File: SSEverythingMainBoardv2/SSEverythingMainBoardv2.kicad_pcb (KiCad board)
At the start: 2 copper layers, 99.1 x 81.3 mm, 70 parts, among them J1 CONN_06SILK_FEMALE_PTH, J2 CONN_06SILK_FEMALE_PTH, J3 POWER, J4 Switch, J5 Conn_01x02, J6 Conn_01x05, M1 Left MOTOR, M2 Right MOTOR, SW1 TACT_SW, U1 DFRobot_DC_Controller

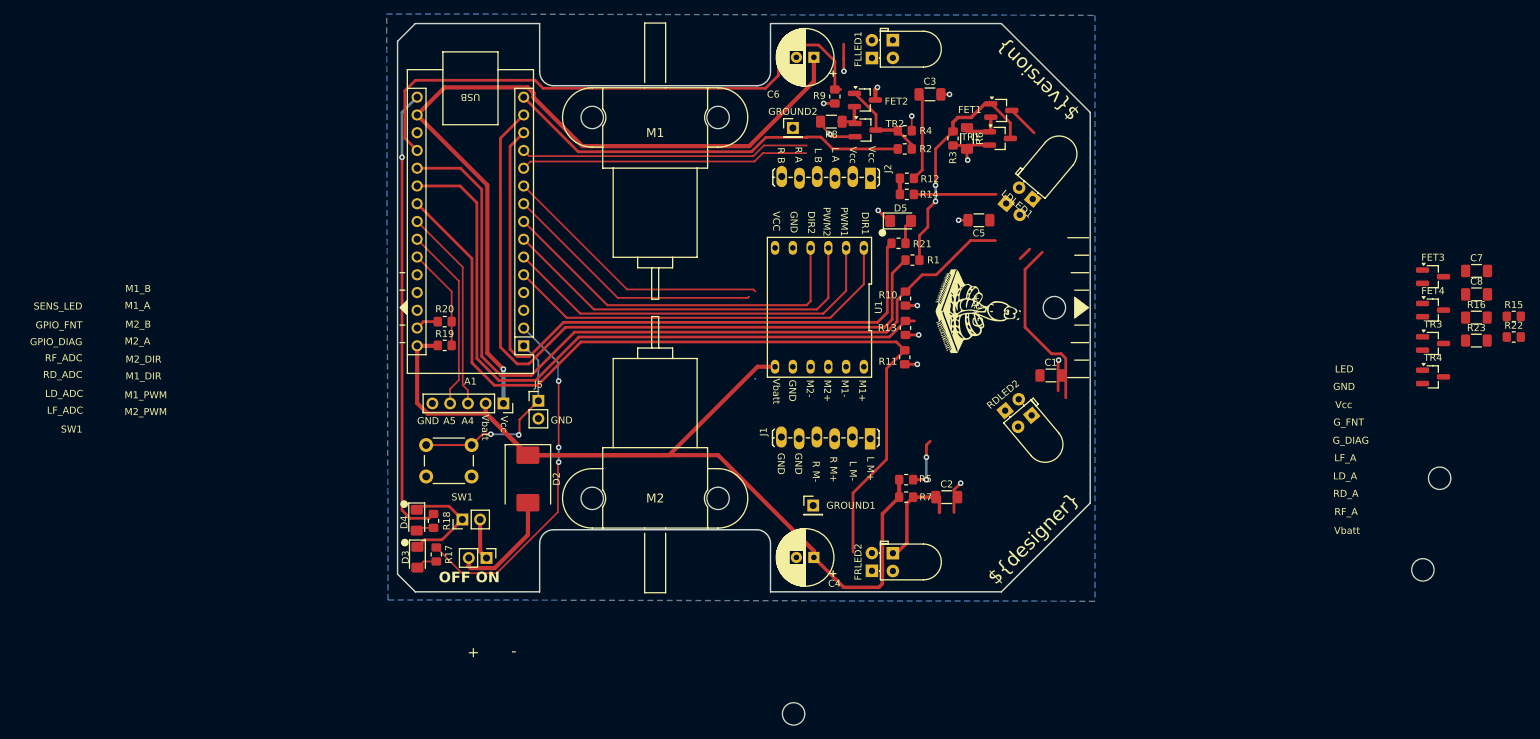
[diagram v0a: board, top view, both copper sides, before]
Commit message: before updating to KiCad 9 and changing sensor design
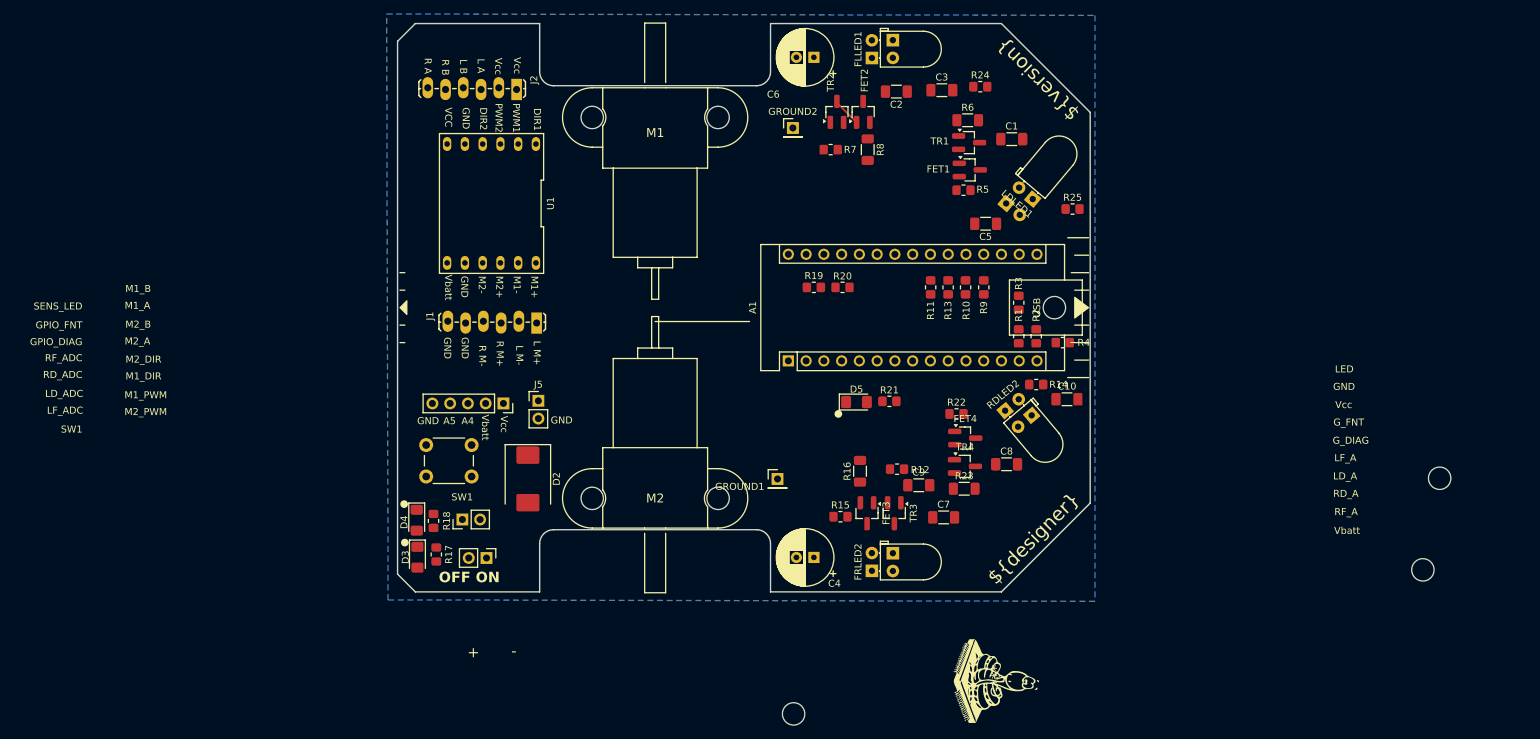
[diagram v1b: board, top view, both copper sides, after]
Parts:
- added C10: 10uF, Capacitor_SMD:C_1206_3216Metric_Pad1.33x1.80mm_HandSolder, F.Cu at (163.9, 118.1)
- added C9: 10uF, Capacitor_SMD:C_1206_3216Metric_Pad1.33x1.80mm_HandSolder, F.Cu at (142.7, 130.4)
- added R24: 220R, Resistor_SMD:R_0805_2012Metric_Pad1.20x1.40mm_HandSolder, F.Cu at (151.5, 73.4)
- added R25: 220R, Resistor_SMD:R_0805_2012Metric_Pad1.20x1.40mm_HandSolder, F.Cu at (164.7, 90.9)
- R15, R22, R5, R7: value 10R -> 220R
- moved R15 100.5 mm to (131.5, 134.9)
- moved R16 90.8 mm to (134.3, 128.4), turned to 90 degrees
- moved FET3 87.7 mm to (135.3, 134.4), turned to -90 degrees
- moved C7 84.0 mm to (146.3, 135.0)
- moved TR3 80.8 mm to (139.2, 134.4), turned to -90 degrees
- moved R22 80.5 mm to (148.1, 120.2)
- moved R23 76.3 mm to (149.2, 130.9)
- moved C8 71.5 mm to (155.3, 127.4)
- moved FET4 69.4 mm to (149.3, 123.7)
- moved TR4 68.2 mm to (149.3, 127.7)
- moved C2 58.4 mm to (139.5, 74.1), turned to 180 degrees
- moved R20 57.1 mm to (131.8, 102.1), turned to 0 degrees
- moved R19 53.4 mm to (127.7, 102.1)
- moved G*** 53.0 mm to (153.8, 158.4)
- moved J2 52.2 mm to (85.2, 73.8)
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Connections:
- A1 pad 5: LEFT_MOTOR_Dir -> RIGHT_MOTOR_Dir
- A1 pad 6: LEFT_MOTOR_PWM -> RIGHT_MOTOR_PWM
- A1 pad 7: RIGHT_MOTOR_PWM -> LEFT_MOTOR_PWM
- A1 pad 8: RIGHT_MOTOR_Dir -> LEFT_MOTOR_Dir
- C3 pad 2: GND -> Net-(C3-Pad2)
- C5 pad 2: GND -> Net-(C5-Pad2)
- J2 pad 5: RIGHT_ENC_A -> RIGHT_ENC_B
- J2 pad 6: RIGHT_ENC_B -> RIGHT_ENC_A
- R10 pad 2: GND -> Net-(C5-Pad2)
- R12 pad 1: Net-(LFPD1-C) -> Net-(RFPD1-C)
- R14 pad 1: Net-(LDPD1-C) -> Net-(RDPD1-C)
- R9 pad 2: GND -> Net-(C3-Pad2)
- RDPD1 pad 1: Net-(LDPD1-C) -> Net-(RDPD1-C)
- RFPD1 pad 1: Net-(LFPD1-C) -> Net-(RFPD1-C)
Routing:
- net Vbatt: track 155.8 -> 0.00 mm
- net RIGHT_FRONT_ADC: track 124.2 -> 0.00 mm
- net LEFT_DIAG_ADC: track 118.8 -> 0.00 mm
- net Vcc: track 118.2 -> 0.00 mm, vias 1 -> 0
- net GPIO_DIAG: track 103.5 -> 0.00 mm
- net RIGHT_DIAG_ADC: track 99.2 -> 0.00 mm
- net SENSOR_LED: track 98.9 -> 0.00 mm
- net LEFT_FRONT_ADC: track 81.7 -> 0.00 mm
- net GND: track 66.1 -> 0.00 mm, vias 11 -> 0
- net Net-(A1-D13/SCK): track 65.2 -> 0.00 mm, vias 1 -> 0
- net LEFT_MOTOR_Dir: track 58.4 -> 0.00 mm
- net GPIO_FRONT: track 58.3 -> 0.00 mm
- net LEFT_MOTOR_PWM: track 57.0 -> 0.00 mm
- net RIGHT_MOTOR_PWM: track 55.6 -> 0.00 mm
- net RIGHT_MOTOR_Dir: track 53.8 -> 0.00 mm
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
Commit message: first draft of new board all layout complete
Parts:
- removed FET1, FET2, FET3, FET4: SOT-23 DMG2302UK-7, Package_TO_SOT_SMD:SOT-23_Handsoldering
- removed R19: 180K, Resistor_SMD:R_0805_2012Metric_Pad1.20x1.40mm_HandSolder
- removed R20: 68K, Resistor_SMD:R_0805_2012Metric_Pad1.20x1.40mm_HandSolder
- removed TR1, TR2, TR3, TR4: BC849, Package_TO_SOT_SMD:SOT-23_Handsoldering
- added G***: LOGO, PBFootPrintLibrary:MicroPythonLogo, F.Cu at (139.7, 88.5)
- added Q1: PBSS4160DS, SamacSys_Parts:SOT95P275X110-6N, F.Cu at (134.8, 75.9)
- added Q2: PBSS4160DS, SamacSys_Parts:SOT95P275X110-6N, F.Cu at (133.7, 133.5)
- added Q3: PBSS4160DS, SamacSys_Parts:SOT95P275X110-6N, F.Cu at (150.4, 78.3)
- added Q4: PBSS4160DS, SamacSys_Parts:SOT95P275X110-6N, F.Cu at (148.8, 131.9)
- LDPD1, LFPD1, RDPD1, RFPD1: moved to F.Cu
- R1, R2: value 220R -> 1K
- R15, R22, R5, R7: value 220R -> 100R
- R16, R23, R6, R8: value R56 -> 2R
- moved R17 62.1 mm to (131.4, 117.4), turned to 0 degrees
- moved D3 60.1 mm to (126.4, 117.4), turned to 0 degrees
- moved R18 58.7 mm to (131.0, 124.9), turned to 0 degrees
- moved D4 56.3 mm to (126.2, 124.9), turned to 0 degrees
- moved J6 51.5 mm to (120.4, 83.0), turned to 0 degrees
- moved G*** 38.6 mm to (141.4, 121.8)
- moved R12 26.5 mm to (165.1, 121.0), turned to 90 degrees
- moved C10 24.1 mm to (144.9, 132.9), turned to 90 degrees
- moved R22 22.7 mm to (129.2, 132.7)
- moved R5 22.5 mm to (129.0, 78.2)
- moved R24 20.8 mm to (165.1, 89.2), turned to -90 degrees
- moved C5 17.6 mm to (146.0, 76.6), turned to -90 degrees
- moved C7 15.4 mm to (132.3, 141.4), turned to 90 degrees
- moved R4 12.9 mm to (152.3, 103.2), turned to 180 degrees
- moved C8 10.4 mm to (144.9, 127.7), turned to 90 degrees
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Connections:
- A1 pad 14: GPIO_DIAG -> GPIO_FRONT
- A1 pad 15: GPIO_FRONT -> GPIO_DIAG
- C3 pad 2: Net-(C3-Pad2) -> GND
- C5 pad 2: Net-(C5-Pad2) -> GND
- R10 pad 2: Net-(C5-Pad2) -> GND
- R9 pad 2: Net-(C3-Pad2) -> GND
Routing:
- net Vcc: track 0.00 -> 179.7 mm, vias 0 -> 1
- net Vbatt: track 0.00 -> 176.7 mm, vias 0 -> 2
- net LEFT_ENC_A: track 0.00 -> 93.8 mm
- net LEFT_ENC_B: track 0.00 -> 93.8 mm
- net RIGHT_ENC_A: track 0.00 -> 93.3 mm
- net RIGHT_ENC_B: track 0.00 -> 93.1 mm
- net GND: track 0.00 -> 92.0 mm, vias 0 -> 11
- net Net-(Q1A-B1): track 4.16 -> 80.1 mm, vias 0 -> 3
- net RIGHT_MOTOR_Dir: track 0.00 -> 72.7 mm
- net LEFT_MOTOR_Dir: track 0.00 -> 72.5 mm
- net LEFT_MOTOR_PWM: track 0.00 -> 72.4 mm
- net RIGHT_MOTOR_PWM: track 0.00 -> 72.2 mm
- net RIGHT_FRONT_ADC: track 0.00 -> 69.3 mm
- net Net-(Q3A-B1): track 0.00 -> 66.0 mm, vias 0 -> 3
- net Net-(A1-D1/TX): track 0.00 -> 56.8 mm
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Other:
- copper layers 2 -> 4
- board text added: "ON"
- board text removed: "OFF ON"

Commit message: First version of v4 board ready for production
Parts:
- M1: footprint ukmarsbot:MINI-METAL-GEARMOTOR-WITH-BRACKET_Alt -> ukmarsbot:MINI-METAL-GEARMOTOR-WITH-BRACKET
- M2: footprint ukmarsbot:MINI-METAL-GEARMOTOR-WITH-BRACKET -> ukmarsbot:MINI-METAL-GEARMOTOR-WITH-BRACKET_Alt
- moved GROUND1 49.9 mm to (72.9, 135.3)
- moved J5 38.9 mm to (125.7, 129.2), turned to 90 degrees
- moved J1 17.6 mm to (73.2, 116.6), turned to 90 degrees
- moved A1 2.85 mm to (121.2, 112.7)
- moved GROUND2 1.77 mm to (123.7, 78.7)
- moved G*** 1.63 mm to (139.8, 121.5)
- moved R18 0.30 mm to (131.3, 124.9)
- moved D3 0.14 mm to (126.3, 117.3)
- moved D4 0.14 mm to (126.3, 125.0)
- turned U1 to 180 degrees
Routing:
- net RIGHT_MOTOR_2: track 8.08 -> 30.9 mm
- net LEFT_MOTOR_Dir: track 72.5 -> 91.9 mm
- net Net-(A1-D1/TX): track 56.8 -> 75.5 mm
- net RIGHT_MOTOR_1: track 8.34 -> 27.1 mm
- net LEFT_MOTOR_2: track 8.08 -> 23.7 mm
- net RIGHT_MOTOR_Dir: track 72.7 -> 60.6 mm
- net LEFT_MOTOR_1: track 8.34 -> 19.9 mm
- net LEFT_MOTOR_PWM: track 72.4 -> 83.6 mm
- net GND: track 92.0 -> 102.8 mm
- net Vbatt: track 176.7 -> 183.8 mm, vias 2 -> 1
- net Net-(Q3A-B1): track 66.0 -> 70.4 mm
- net Vcc: track 179.7 -> 183.9 mm
- net LEFT_DIAG_ADC: track 28.9 -> 25.1 mm
- net RIGHT_MOTOR_PWM: track 72.2 -> 75.7 mm
- net SENSOR_LED: track 25.6 -> 22.7 mm
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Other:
- board text added: "L DIR"
- board text added: "L PWM"
- board text added: "R DIR"
- board text added: "R PWM"
- board text removed: "GPIO_DIAG"
- board text removed: "GPIO_FNT"
- board text removed: "LD_ADC"
- board text removed: "LED"
- board text removed: "LF_ADC"
- board text removed: "M1_A"
- board text removed: "M1_B"
- board text removed: "M1_DIR"
- board text removed: "M1_PWM"
- board text removed: "M2_A"
- board text removed: "M2_B"
- board text removed: "M2_DIR"
- board text removed: "M2_PWM"
- board text removed: "RD_ADC"
- board text removed: "RF_ADC"
- board text removed: "SENS_LED"
- board text removed: "SW1"

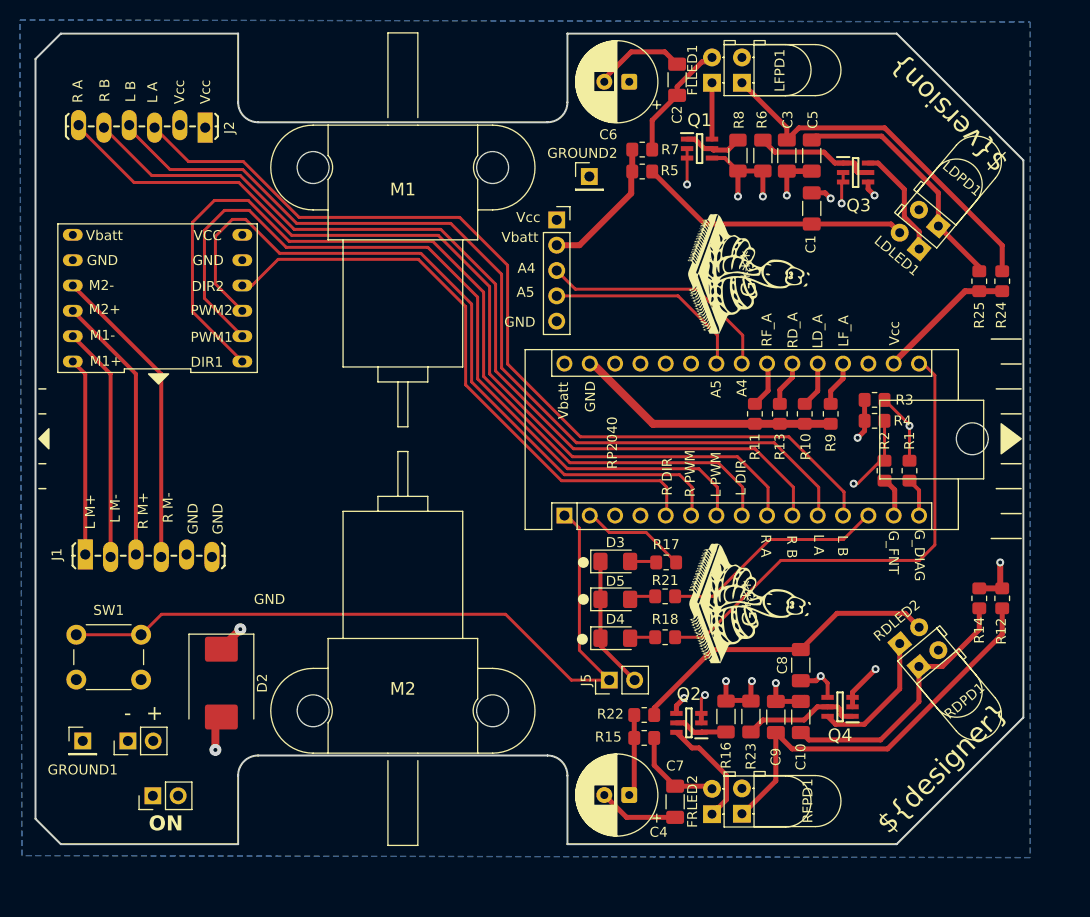
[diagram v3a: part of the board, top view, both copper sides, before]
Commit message: updated sensor locations, all resistors are back to be 0805, routing changes and moved the motor controller around plus other changes from Peter's suggestions
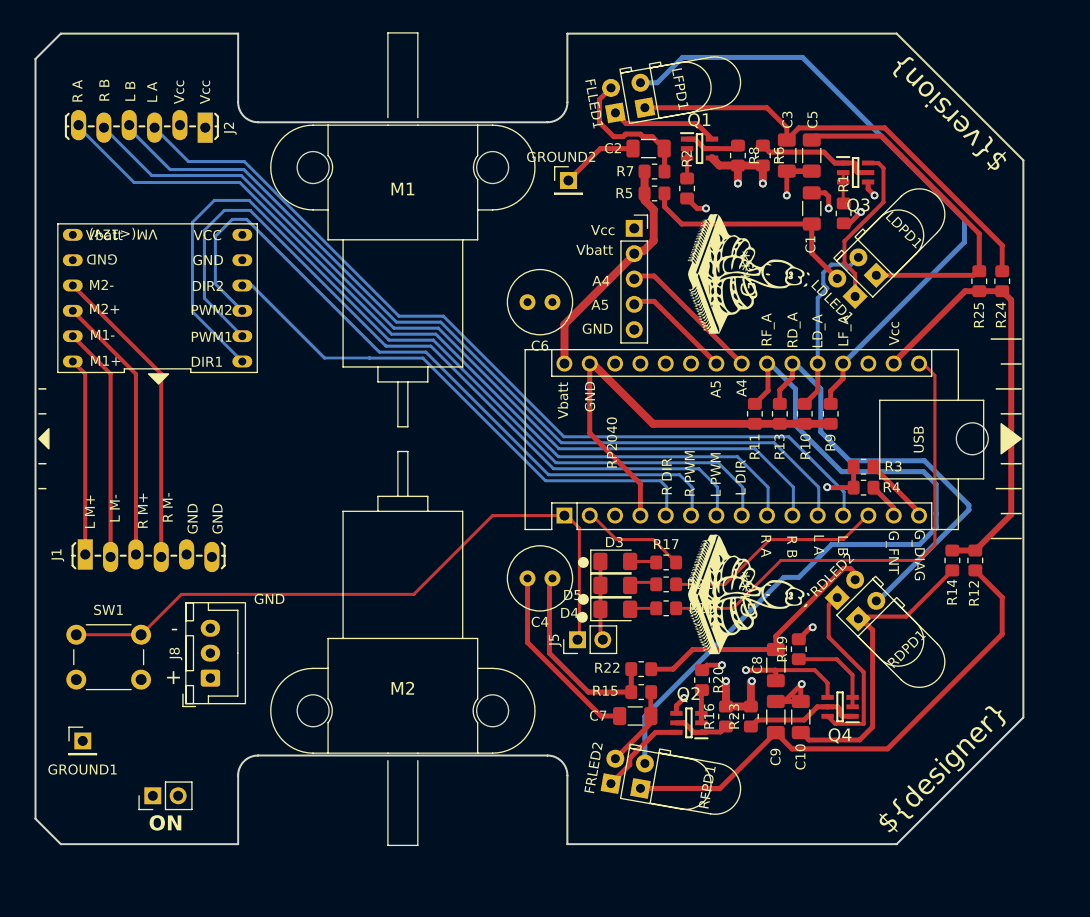
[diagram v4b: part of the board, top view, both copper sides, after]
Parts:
- removed D2: SS34, Diode_SMD:D_SMC
- removed J3: POWER, Connector_PinHeader_2.54mm:PinHeader_1x02_P2.54mm_Vertical
- added G***: LOGO, PBFootPrintLibrary:MicroPythonLogo, B.Cu at (80.7, 105.5)
- added J8: Conn_01x03, Connector_JST:JST_XH_B3B-XH-A_1x03_P2.50mm_Vertical, F.Cu at (85.7, 129.0)
- added R19: 1K, Resistor_SMD:R_0805_2012Metric_Pad1.20x1.40mm_HandSolder, F.Cu at (144.7, 126.1)
- added R20: 1K, Resistor_SMD:R_0805_2012Metric_Pad1.20x1.40mm_HandSolder, F.Cu at (135.0, 129.2)
- C4, C6: footprint Capacitor_THT:CP_Radial_D8.0mm_P2.50mm -> Capacitor_THT:C_Radial_D6.3mm_H7.0mm_P2.50mm
- R10, R11, R13, R9: value R -> 2K2
- R16, R23, R6, R8: value 2R -> 4R7; footprint Resistor_SMD:R_1206_3216Metric_Pad1.30x1.75mm_HandSolder -> Resistor_SMD:R_0805_2012Metric_Pad1.20x1.40mm_HandSolder
- moved R2 34.5 mm to (133.5, 79.9)
- moved R1 26.6 mm to (149.2, 82.4)
- moved C6 23.4 mm to (120.0, 91.3)
- moved C4 23.0 mm to (120.0, 119.0)
- moved FRLED2 10.6 mm to (125.9, 139.6), turned to 80 degrees
- moved RFPD1 10.5 mm to (128.8, 140.1), turned to 80 degrees
- moved FLLED1 10.1 mm to (126.3, 72.3), turned to 100 degrees
- moved LFPD1 10.0 mm to (129.3, 71.8), turned to 100 degrees
- moved C7 9.48 mm to (128.3, 132.8), turned to 0 degrees
- moved LDLED1 7.99 mm to (150.4, 90.7), turned to 135 degrees
- moved LDPD1 7.94 mm to (152.5, 88.6), turned to 135 degrees
- moved J6 7.82 mm to (128.2, 83.9)
- moved RDLED2 7.78 mm to (148.6, 120.9), turned to 45 degrees
- moved RDPD1 7.73 mm to (150.7, 123.1), turned to 45 degrees
- moved C2 7.47 mm to (129.6, 75.9), turned to 0 degrees
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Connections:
- J4 pad 2: /PWR -> Vbatt
- Q2 pad 2: Net-(Q1A-B1) -> Net-(Q2A-B1)
- Q2 pad 3: Net-(Q1A-B1) -> Net-(Q2A-B1)
- Q4 pad 2: Net-(Q3A-B1) -> Net-(Q4A-B1)
- Q4 pad 3: Net-(Q3A-B1) -> Net-(Q4A-B1)
- R3 pad 1: Net-(Q3A-B1) -> GPIO_DIAG
- R4 pad 1: Net-(Q1A-B1) -> GPIO_FRONT
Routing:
- net Net-(Q1A-B1): track 80.8 -> 3.00 mm, vias 3 -> 0
- net GPIO_FRONT: track 4.02 -> 80.1 mm, vias 0 -> 2
- net Net-(Q3A-B1): track 70.4 -> 3.12 mm, vias 3 -> 0
- net GPIO_DIAG: track 3.90 -> 67.6 mm, vias 0 -> 2
- net Vcc: track 183.9 -> 135.8 mm, vias 1 -> 0
- net GND: track 102.8 -> 137.8 mm
- net LEFT_FRONT_ADC: track 53.1 -> 64.3 mm
- net Net-(RFPD1-C): track 40.3 -> 51.6 mm
- net Net-(LDPD1-C): track 24.8 -> 35.7 mm
- net /PWR: track 9.70 -> 0.00 mm, vias 1 -> 0
- net Net-(A1-SDA/A4): track 24.2 -> 14.5 mm
- net Net-(A1-SCL/A5): track 20.6 -> 10.9 mm
- net Net-(Q4A-B1): track 0.00 -> 9.24 mm
- net /PWR_IN: track 5.52 -> 14.2 mm
- net Net-(LFPD1-C): track 37.2 -> 45.9 mm
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- added copper zone on In2.Cu, net GND
- removed copper zone on B.Cu, net GND

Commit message: routing changes
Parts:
- moved R25 5.04 mm to (159.6, 93.1)
- moved R24 5.04 mm to (161.9, 93.1)
- moved R10 3.60 mm to (148.9, 102.4)
- moved R9 1.20 mm to (146.7, 102.4)
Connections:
- A1 pad 19: LEFT_FRONT_ADC -> LEFT_DIAG_ADC
- A1 pad 20: LEFT_DIAG_ADC -> LEFT_FRONT_ADC
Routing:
- net GND: track 137.8 -> 243.6 mm
- net LEFT_FRONT_ADC: track 64.3 -> 40.3 mm
- net Vcc: track 135.8 -> 128.5 mm
- net Net-(RFPD1-C): track 51.6 -> 48.0 mm
- net Net-(LFPD1-C): track 45.9 -> 48.4 mm
- net RIGHT_DIAG_ADC: track 44.0 -> 41.9 mm
- net LEFT_DIAG_ADC: track 18.8 -> 18.2 mm
